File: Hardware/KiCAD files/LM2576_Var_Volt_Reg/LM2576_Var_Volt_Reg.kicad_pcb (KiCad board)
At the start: 2 copper layers, 48 x 48 mm, 14 parts, among them J1 Conn_01x03_Pin, U2 LM2576HVS-ADJ

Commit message: general update stuff
- updated PCBs
- removed marlin submodule
- played with firmware
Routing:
- net /Vin: track 63.4 -> 66.7 mm
- net /Vout: track 53.7 -> 56.0 mm

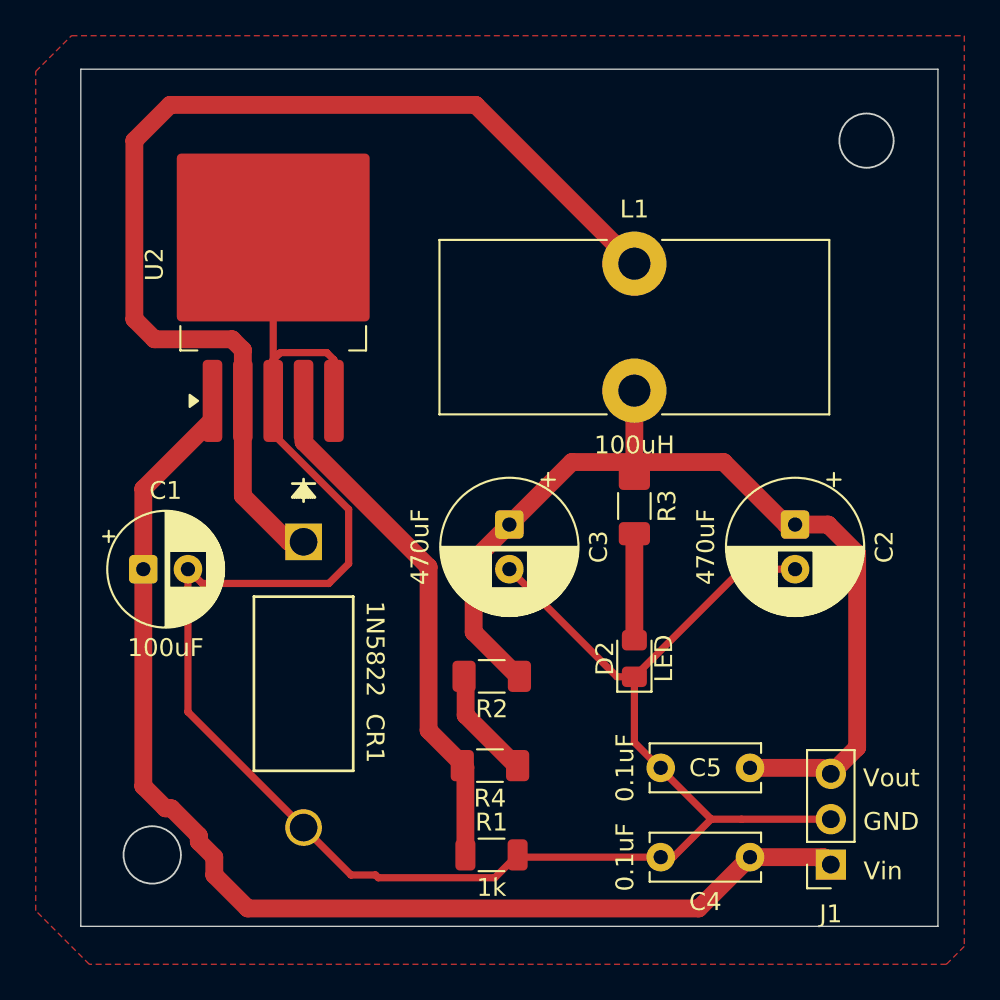
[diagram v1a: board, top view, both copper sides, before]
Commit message: 1st push of PCB's for printing
This is pre-peer review. This almost certainly has section that need adjustment. also realized I'm missing the USB-Uart bridge. first thing added in next version.
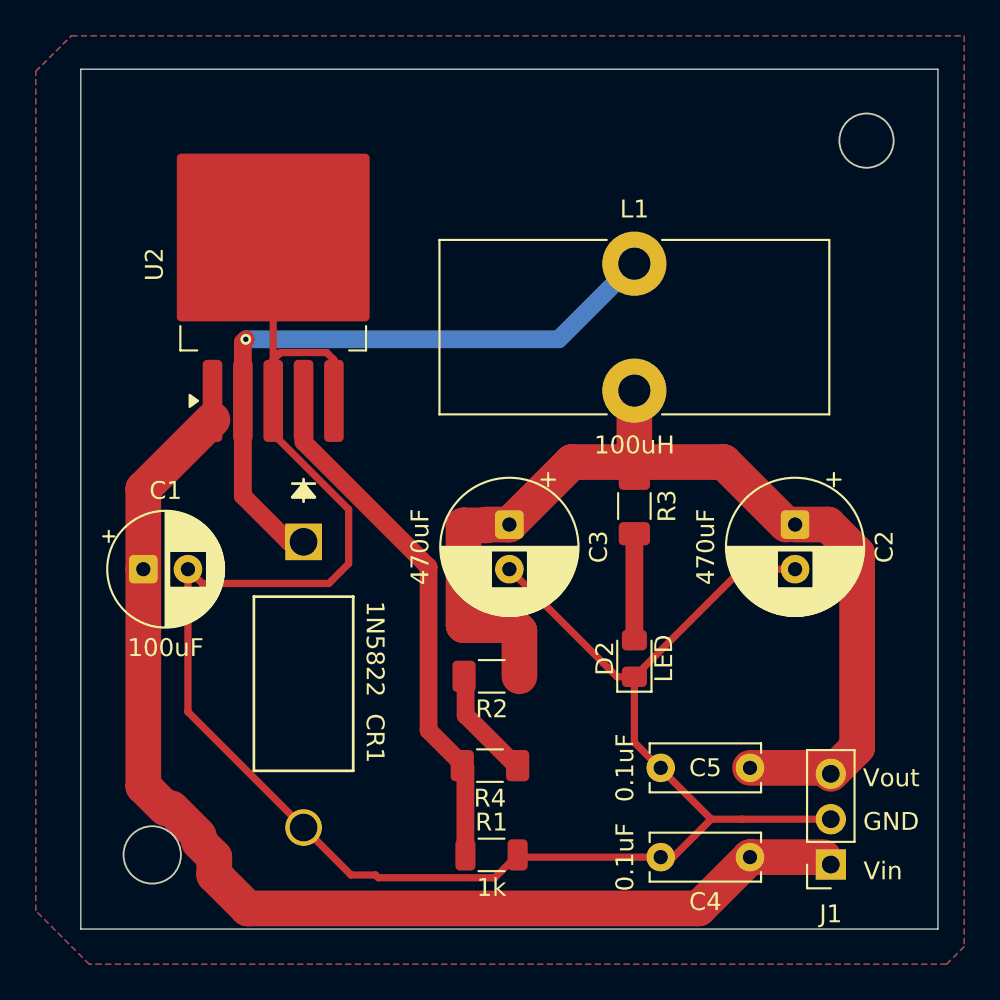
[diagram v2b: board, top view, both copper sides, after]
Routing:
- net Net-(U2-OUT): track 61.9 -> 36.8 mm, vias 0 -> 1
- net /Vout: track 56.0 -> 59.6 mm
- added copper zone on B.Cu, net GND
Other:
- board size 48 x 48 mm -> 48 x 48.2 mm

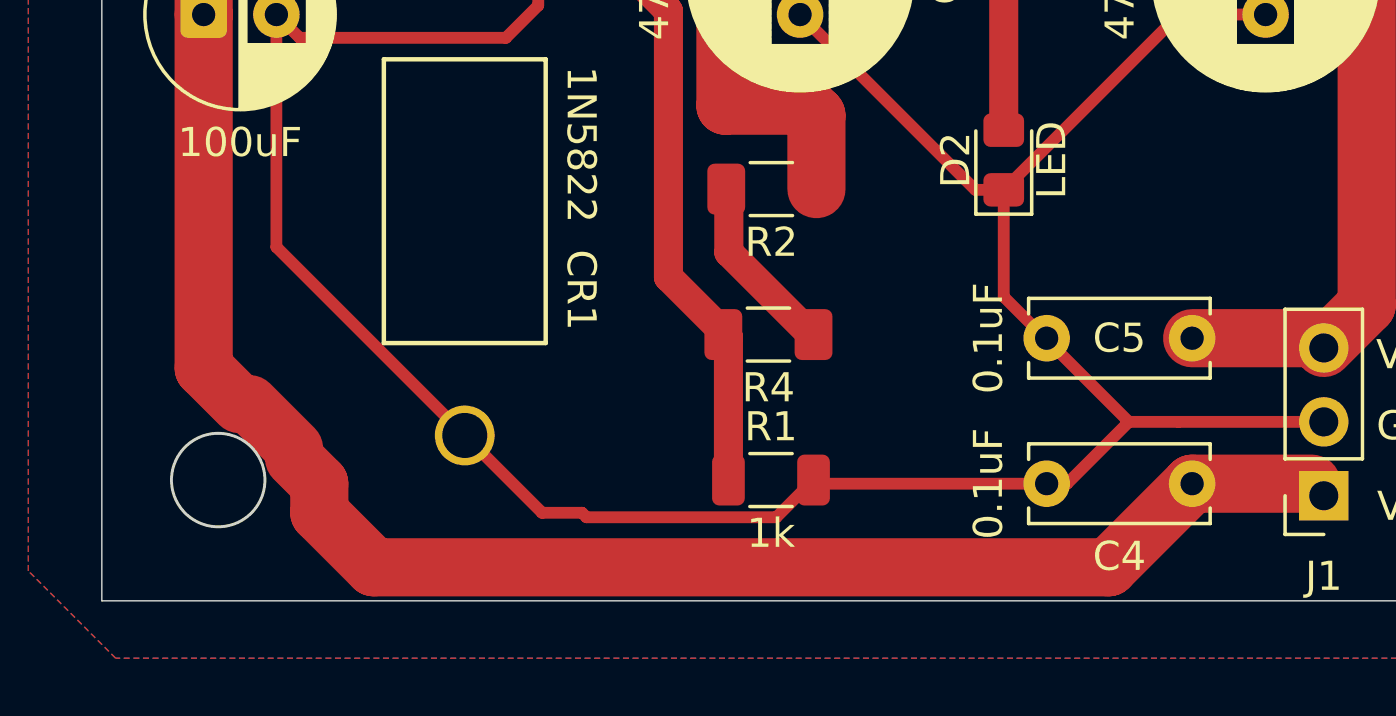
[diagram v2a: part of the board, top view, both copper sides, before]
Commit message: general progress and adjustments
new footprint for pi reg inductor, var reg checked concurred with current part and value. re footprinted motor driver. started swapping head. adjusted some device footprints.
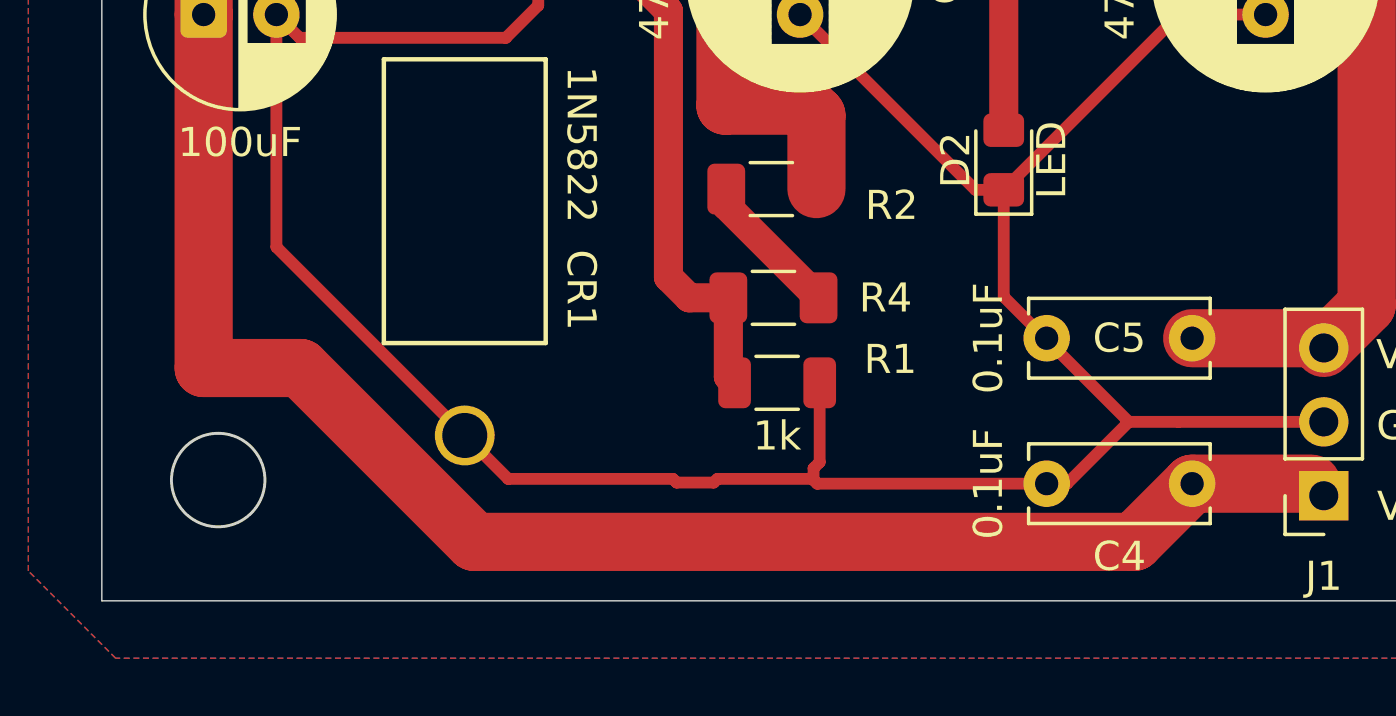
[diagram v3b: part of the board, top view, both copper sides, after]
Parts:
- moved R1 3.35 mm to (173.7, 73.5)
- moved R4 1.27 mm to (173.6, 70.6)
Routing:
- net GND: track 123.0 -> 125.5 mm
- net /FB: track 29.2 -> 26.7 mm
- net /Vin: track 66.7 -> 65.2 mm
- net Net-(R2-Pad2): track 6.17 -> 5.05 mm
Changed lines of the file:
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@@
 	(footprint "Resistor_SMD:R_1206_3216Metric_Pad1.30x1.75mm_HandSolder"
 		(layer "F.Cu")
-		(at 173.4375 71.875 180)
+		(at 173.609 70.612 180)
 		(descr "Resistor SMD 1206 (3216 Metric), square (rectangular) end terminal, IPC-7351 nominal with elongated pad for handsoldering. (Body size source: IPC-SM-782 page 72, https://www.pcb-3d.com/wordpress/wp-content/uploads/ipc-sm-782a_amendment_1_and_2.pdf), generated with kicad-footprint-generator")
 		(tags "resistor handsolder")
 		(property "Reference" "R4"
-			(at 0 -1.83 180)
+			(at -3.8545 -0.007 180)
 			(layer "F.SilkS")
 			(effects
@@
 		(tags "resistor handsolder")
 		(property "Reference" "R2"
-			(at 0 -1.83 180)
+			(at -4.1355 -0.562 180)
 			(layer "F.SilkS")
 			(effects
@@
 		)
 		(property "Value" "Rvar"
-			(at 0 1.83 180)
+			(at 0.1825 1.851 180)
 			(layer "F.Fab")
 			(effects
@@
 	(footprint "Resistor_SMD:R_1206_3216Metric"
 		(layer "F.Cu")
-		(at 173.525 76.875)
+		(at 173.736 73.533)
 		(descr "Resistor SMD 1206 (3216 Metric), square (rectangular) end terminal, IPC-7351 nominal, (Body size source: IPC-SM-782 page 72, https://www.pcb-3d.com/wordpress/wp-content/uploads/ipc-sm-782a_amendment_1_and_2.pdf), generated with kicad-footprint-generator")
 		(tags "resistor")
 		(property "Reference" "R1"
-			(at 0 -1.83 0)
+			(at 3.894 -0.802 0)
 			(layer "F.SilkS")
 			(effects
@@
 	)
 	(segment
+		(start 171.557692 76.962)
+		(end 171.684692 76.835)
+		(width 0.4064)
+		(layer "F.Cu")
+		(net "GND")
+	)
+	(segment
+		(start 156.525 68.86735)
+		(end 164.49265 76.835)
+		(width 0.4064)
+		(layer "F.Cu")
+		(net "GND")
+	)
+	(segment
+		(start 174.9875 76.875)
+		(end 174.9875 76.4725)
+		(width 0.4064)
+		(layer "F.Cu")
+		(net "GND")
+	)
+	(segment
 		(start 165.525 57.525)
 		(end 165.525 60.5634)
@@
 	)
 	(segment
-		(start 156.525 60.875)
-		(end 156.525 68.86735)
+		(start 164.49265 76.835)
+		(end 170.154308 76.835)
 		(width 0.4064)
 		(layer "F.Cu")
@@
 	)
 	(segment
-		(start 156.525 68.86735)
-		(end 165.65765 78)
-		(width 0.4064)
-		(layer "F.Cu")
-		(net "GND")
-	)
-	(segment
 		(start 164.7 51.45)
 		(end 164.7 49.15)
@@
 	)
 	(segment
+		(start 156.525 60.875)
+		(end 156.525 68.86735)
+		(width 0.4064)
+		(layer "F.Cu")
+		(net "GND")
+	)
+	(segment
 		(start 183.7 77)
 		(end 175.1125 77)
@@
 	)
 	(segment
-		(start 167.03 78)
-		(end 167.1842 78.1542)
+		(start 161.3 42.3)
+		(end 161.3 51.45)
 		(width 0.4064)
 		(layer "F.Cu")
@@
 	)
 	(segment
-		(start 161.3 42.3)
-		(end 161.3 51.45)
+		(start 175.1985 76.2615)
+		(end 175.1985 73.533)
 		(width 0.4064)
 		(layer "F.Cu")
@@
 	)
 	(segment
-		(start 175.1125 77)
-		(end 174.9875 76.875)
+		(start 174.9875 76.4725)
+		(end 175.1985 76.2615)
 		(width 0.4064)
 		(layer "F.Cu")
@@
 	)
 	(segment
-		(start 167.1842 78.1542)
-		(end 173.7083 78.1542)
+		(start 175.1125 77)
+		(end 174.9875 76.875)
 		(width 0.4064)
 		(layer "F.Cu")
@@
 	)
 	(segment
-		(start 165.65765 78)
-		(end 167.03 78)
+		(start 170.281308 76.962)
+		(end 171.557692 76.962)
 		(width 0.4064)
 		(layer "F.Cu")
@@
 	)
 	(segment
+		(start 170.154308 76.835)
+		(end 170.281308 76.962)
+		(width 0.4064)
+		(layer "F.Cu")
+		(net "GND")
+	)
+	(segment
 		(start 161.3 51.45)
 		(end 161.3 53.3)
@@
 	)
 	(segment
+		(start 171.684692 76.835)
+		(end 174.9475 76.835)
+		(width 0.4064)
+		(layer "F.Cu")
+		(net "GND")
+	)
+	(segment
 		(start 181.525 70.575)
 		(end 185.825 74.875)
@@
 	)
 	(segment
-		(start 173.7083 78.1542)
+		(start 174.9475 76.835)
 		(end 174.9875 76.875)
 		(width 0.4064)
@@
 	)
 	(segment
-		(start 172.075 69.05)
-		(end 174.9 71.875)
+		(start 171.9875 66.875)
+		(end 171.9875 67.4405)
 		(width 1)
 		(layer "F.Cu")
@@
 	)
 	(segment
-		(start 172.075 66.875)
-		(end 172.075 69.05)
+		(start 171.9875 67.4405)
+		(end 175.159 70.612)
 		(width 1)
 		(layer "F.Cu")
@@
 	)
 	(segment
-		(start 170 69.9)
-		(end 170 60.75)
+		(start 172.059 70.612)
+		(end 172.059 73.3185)
 		(width 1)
 		(layer "F.Cu")
@@
 	)
 	(segment
-		(start 163 53.75)
-		(end 163 51.45)
+		(start 170.712 70.612)
+		(end 172.059 70.612)
 		(width 1)
 		(layer "F.Cu")
@@
 	)
 	(segment
-		(start 172.0625 76.875)
-		(end 172.0625 71.9625)
+		(start 170 69.9)
+		(end 170 60.75)
 		(width 1)
 		(layer "F.Cu")
@@
 	)
 	(segment
-		(start 172.0625 71.9625)
-		(end 170 69.9)
+		(start 163 53.75)
+		(end 163 51.45)
 		(width 1)
 		(layer "F.Cu")
@@
 	)
 	(segment
-		(start 154.025 56.375)
-		(end 154.025 60.875)
-		(width 2)
-		(layer "F.Cu")
-		(net "/Vin")
-	)
-	(segment
-		(start 158 78)
-		(end 159.874 79.874)
-		(width 2)
+		(start 170 69.9)
+		(end 170.712 70.612)
+		(width 1)
 		(layer "F.Cu")
-		(net "/Vin")
+		(net "/FB")
 	)
 	(segment
-		(start 159.874 79.874)
-		(end 185.126 79.874)
-		(width 2)
+		(start 172.059 73.3185)
+		(end 172.2735 73.533)
+		(width 1)
 		(layer "F.Cu")
-		(net "/Vin")
+		(net "/FB")
 	)
 	(segment
-		(start 154.025 73.025)
-		(end 155.267514 74.267514)
+		(start 154.025 56.375)
+		(end 154.025 60.875)
 		(width 2)
 		(layer "F.Cu")
@@
 	)
 	(segment
-		(start 157.132486 75.794943)
-		(end 157.132486 76.132486)
-		(width 1)
-		(layer "F.Cu")
-		(net "/Vin")
-	)
-	(segment
-		(start 155.267514 74.267514)
-		(end 155.605057 74.267514)
-		(width 1.5)
+		(start 157.353 73.025)
+		(end 163.328 79)
+		(width 2)
 		(layer "F.Cu")
 		(net "/Vin")
 	)
 	(segment
-		(start 154.025 60.875)
-		(end 154.025 73.025)
+		(start 186 79)
+		(end 188 77)
 		(width 2)
 		(layer "F.Cu")
@@
 	)
 	(segment
-		(start 155.605057 74.267514)
-		(end 157.132486 75.794943)
+		(start 154.025 73.025)
+		(end 157.353 73.025)
 		(width 2)
 		(layer "F.Cu")
@@
 	)
 	(segment
-		(start 158 77)
-		(end 158 78)
+		(start 188 77)
+		(end 192.11 77)
 		(width 2)
 		(layer "F.Cu")
@@
 	)
 	(segment
-		(start 188 77)
-		(end 192.11 77)
+		(start 163.328 79)
+		(end 186 79)
 		(width 2)
 		(layer "F.Cu")
@@
 	)
 	(segment
-		(start 185.126 79.874)
-		(end 188 77)
+		(start 154.025 60.875)
+		(end 154.025 73.025)
 		(width 2)
 		(layer "F.Cu")
@@
 		(layer "F.Cu")
 		(net "/Vin")
-	)
-	(segment
-		(start 157.132486 76.132486)
-		(end 158 77)
-		(width 2)
-		(layer "F.Cu")
-		(net "/Vin")
